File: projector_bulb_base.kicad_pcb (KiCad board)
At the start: 2 copper layers, 31 x 31 mm, 11 parts, among them J1 AC_1, J10 mount_2, J3 AC_2, J9 mount_1

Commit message: Revision 2, still needs documentation and things
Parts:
- C1, C2: footprint Capacitor_THT:CP_Radial_D16.0mm_P7.50mm -> Capacitor_THT:CP_Radial_D12.5mm_P5.00mm
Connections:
- J10 pad 1: Net-(J10-Pad1) -> (no net)
- J9 pad 1: Net-(J9-Pad1) -> (no net)
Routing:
- net GND: track 15.8 -> 30.3 mm

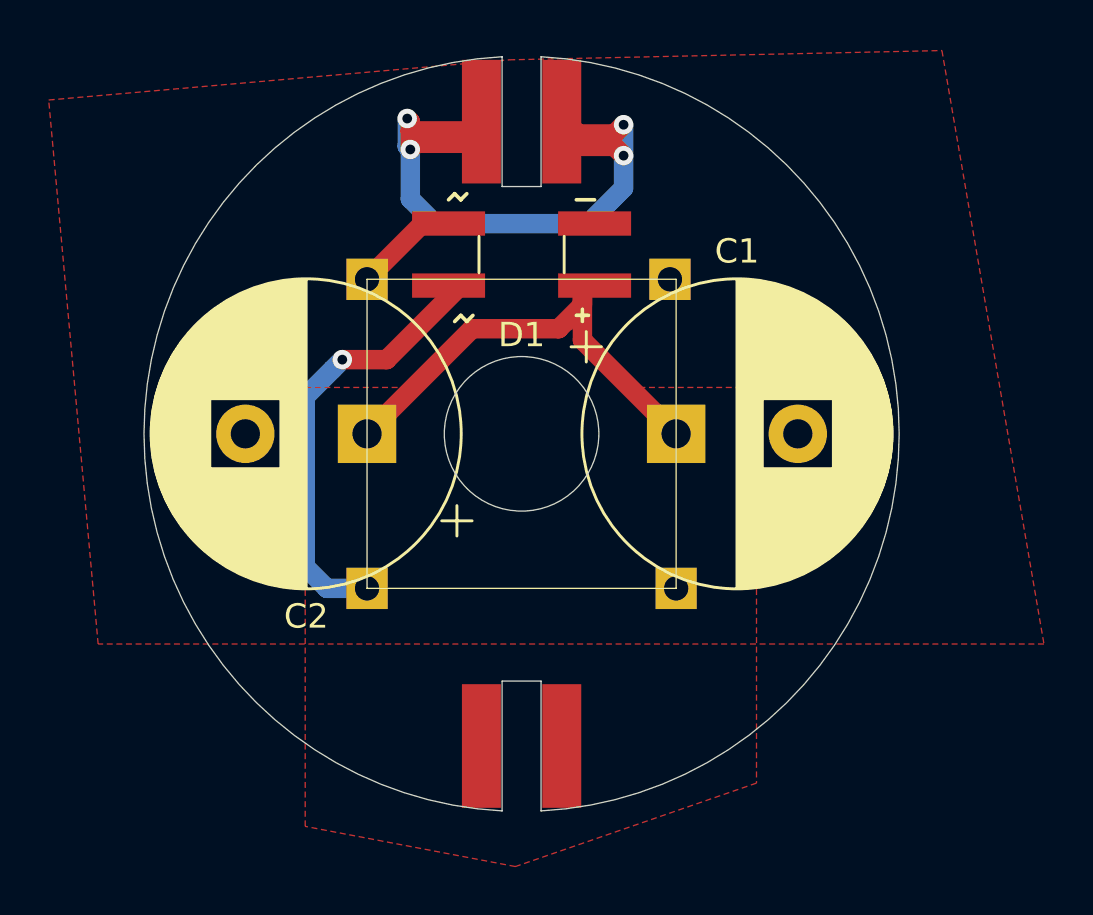
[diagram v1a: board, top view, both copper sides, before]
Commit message: Much progress on Aluminum PCB
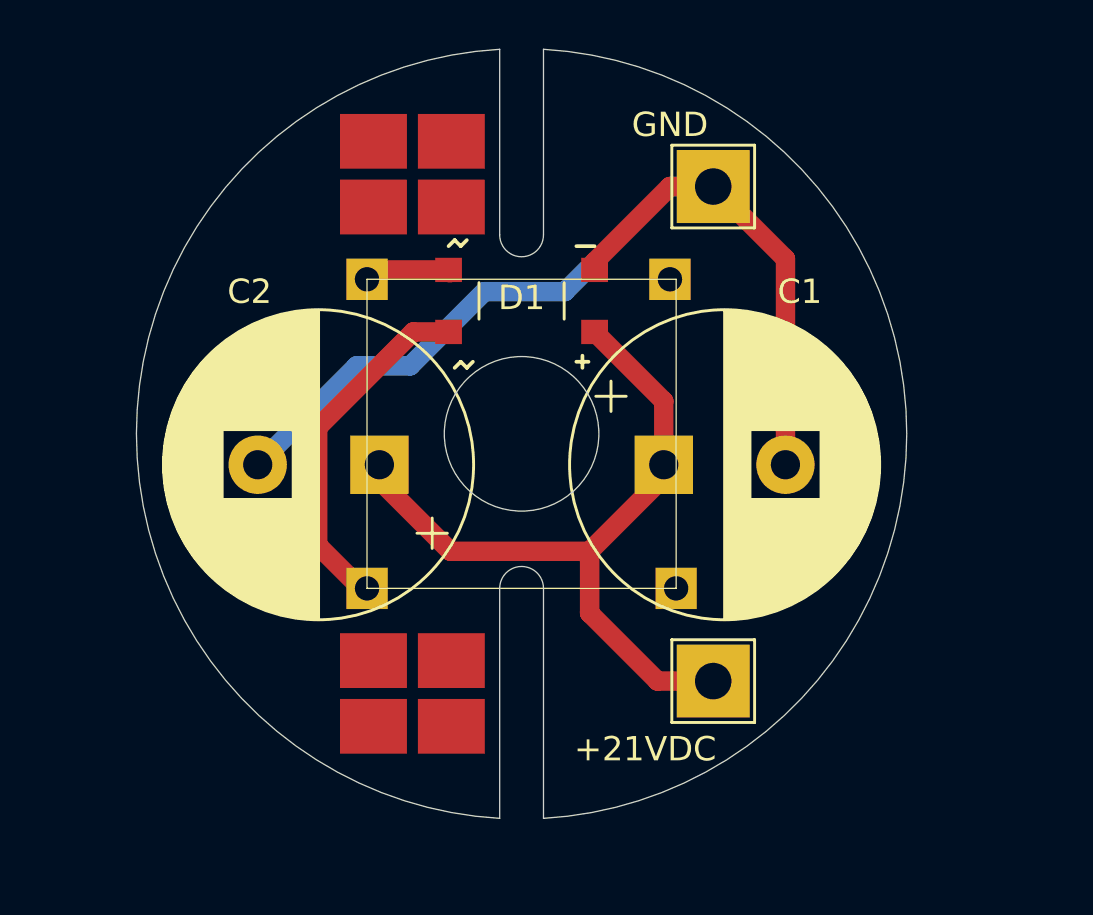
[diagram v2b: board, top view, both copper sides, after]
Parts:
- removed REF** (x4): angle_joint, projector_bulb:angle_joint
- added +21VDC: to_upright_+, TestPoint:TestPoint_THTPad_3.0x3.0mm_Drill1.5mm, F.Cu at (84.1, 86.4)
- added GND: to_upright_-, TestPoint:TestPoint_THTPad_3.0x3.0mm_Drill1.5mm, F.Cu at (84.1, 66.0)
- added J11: mount_2, projector_bulb:wuerth_7466303R, F.Cu at (71.7, 65.5)
- added J12: mount_1, projector_bulb:wuerth_7466303R, F.Cu at (71.7, 86.9)
- C1, C2: value 2200u -> 1000μ
- moved D1 1.91 mm to (76.2, 70.7)
- moved C2 1.37 mm to (70.4, 77.5)
- moved C1 1.37 mm to (82.0, 77.5)
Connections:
- net GND renamed GND_BASE
- net Net-(C1-Pad1) renamed VIN_BASE
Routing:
- net GND_BASE: track 30.3 -> 42.6 mm, vias 4 -> 0
- net VIN_BASE: track 19.5 -> 29.3 mm
- net Net-(D1-Pad4): track 18.2 -> 14.6 mm, vias 1 -> 0
- net Net-(D1-Pad3): track 4.80 -> 3.61 mm
- removed copper zone on F.Cu, net GND_BASE
- removed copper zone on F.Cu, net VIN_BASE
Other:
- board size 31 x 31 mm -> 31.7 x 31.6 mm

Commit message: Add test points, replaced some expensive components with cheaper alternatives
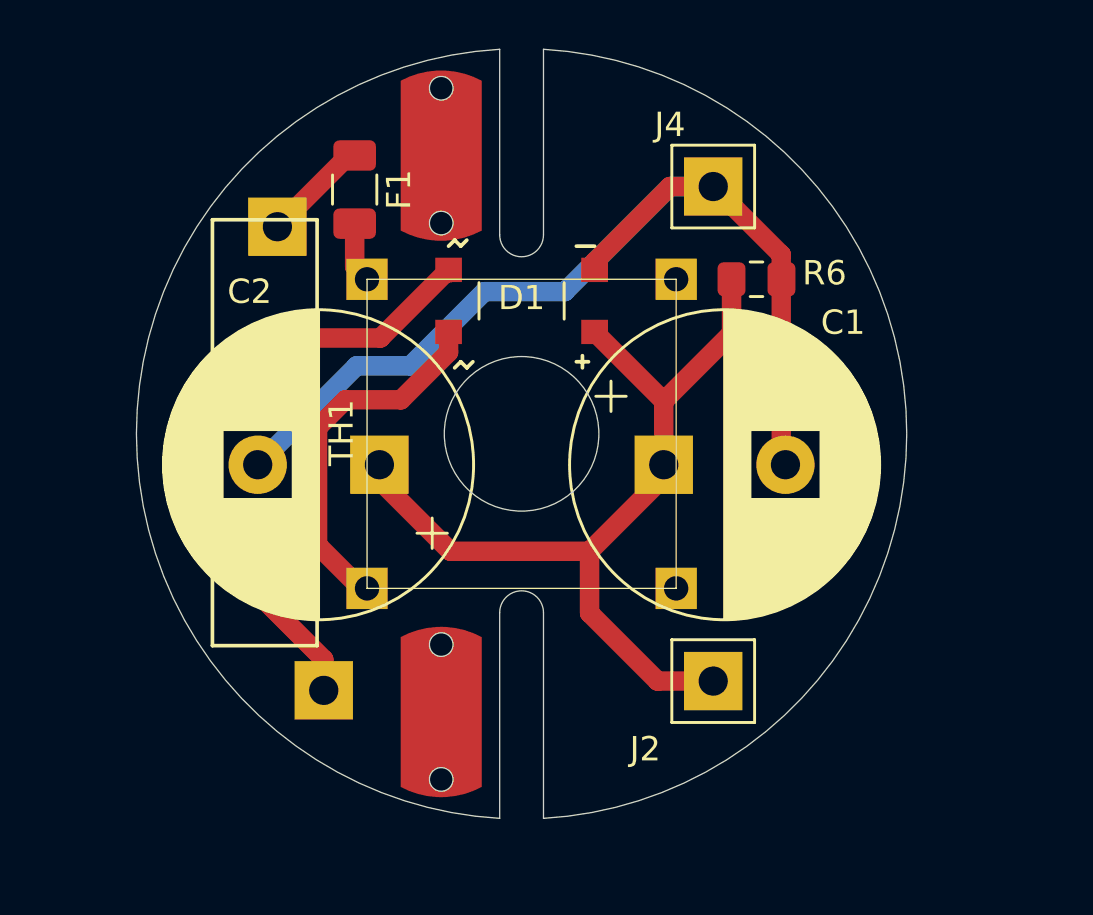
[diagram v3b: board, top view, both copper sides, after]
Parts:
- removed J1: AC_1, Connector_PinSocket_2.54mm:PinSocket_1x01_P2.54mm_Vertical
- removed J10: mount_2, Connector_PinSocket_2.54mm:PinSocket_1x01_P2.54mm_Vertical
- removed J11: mount_2, projector_bulb:wuerth_7466303R
- removed J12: mount_1, projector_bulb:wuerth_7466303R
- removed J3: AC_2, Connector_PinSocket_2.54mm:PinSocket_1x01_P2.54mm_Vertical
- removed J9: mount_1, Connector_PinSocket_2.54mm:PinSocket_1x01_P2.54mm_Vertical
- added F1: Fuse, Fuse:Fuse_1206_3216Metric, F.Cu at (69.3, 66.2)
- added H1: MountingHole, projector_bulb:wuerth_7466310R, F.Cu at (72.9, 64.8)
- added H2: MountingHole, projector_bulb:wuerth_7466310R, F.Cu at (72.9, 87.6)
- added LA1: Lamp, projector_bulb:GX17q, B.Cu at (76.2, 76.2)
- added R6: 1M, Resistor_SMD:R_0805_2012Metric_Pad1.15x1.40mm_HandSolder, F.Cu at (85.9, 69.8)
- added TH1: Thermistor_NTC, Varistor:RV_Disc_D21.5mm_W4.3mm_P10mm, F.Cu at (64.9, 81.2)
- renumbered +21VDC to J2, GND to J4
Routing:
- net Net-(D1-Pad3): track 3.61 -> 26.6 mm
- net VIN_BASE: track 29.3 -> 35.5 mm
- net Net-(F1-Pad1): track 0.00 -> 4.39 mm
- net Net-(F1-Pad2): track 0.00 -> 2.50 mm
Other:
- outline, holes or cut-outs redrawn

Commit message: BOM and readme updated
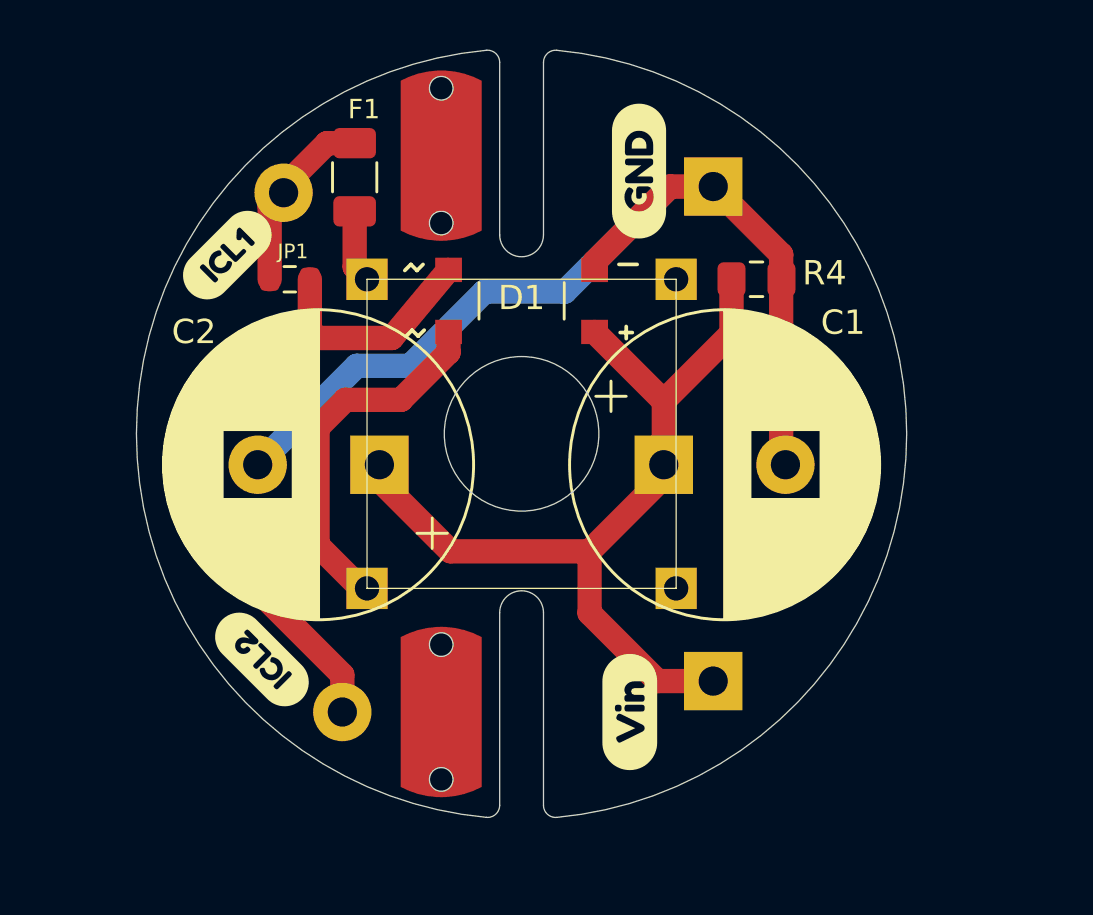
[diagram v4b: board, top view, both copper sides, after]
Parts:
- added JP1: ICL Bypass, Resistor_SMD:R_0603_1608Metric, F.Cu at (66.7, 69.8)
- added svg2mod: G***, label, F.Cu at (81.0, 65.4)
- added svg2mod: G***, label, F.Cu at (80.6, 87.6)
- added svg2mod: G***, label, F.Cu at (65.5, 85.5)
- added svg2mod: G***, label, F.Cu at (63.8, 70.0)
- D1: value D_Bridge_+-AA -> Bridge Rectifier
- moved TH1 0.89 mm to (64.9, 82.0)
- moved F1 0.50 mm to (69.3, 65.7)
- renumbered J2 to J1, J4 to J2, R6 to R4
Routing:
- net Net-(D1-Pad3): track 26.6 -> 30.3 mm
- net Net-(F1-Pad1): track 4.39 -> 7.27 mm
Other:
- board size 31.7 x 31.6 mm -> 31.6 x 31.5 mm
- net class Base Track added: clearance 0.25, trace_width 1, via_dia 0.8, via_drill 0.4
- rule pad_to_mask_clearance: 0.05 -> 0

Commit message: Locking in revision 3 finally; moved the optional ICL to a place where I can treat it like a test point
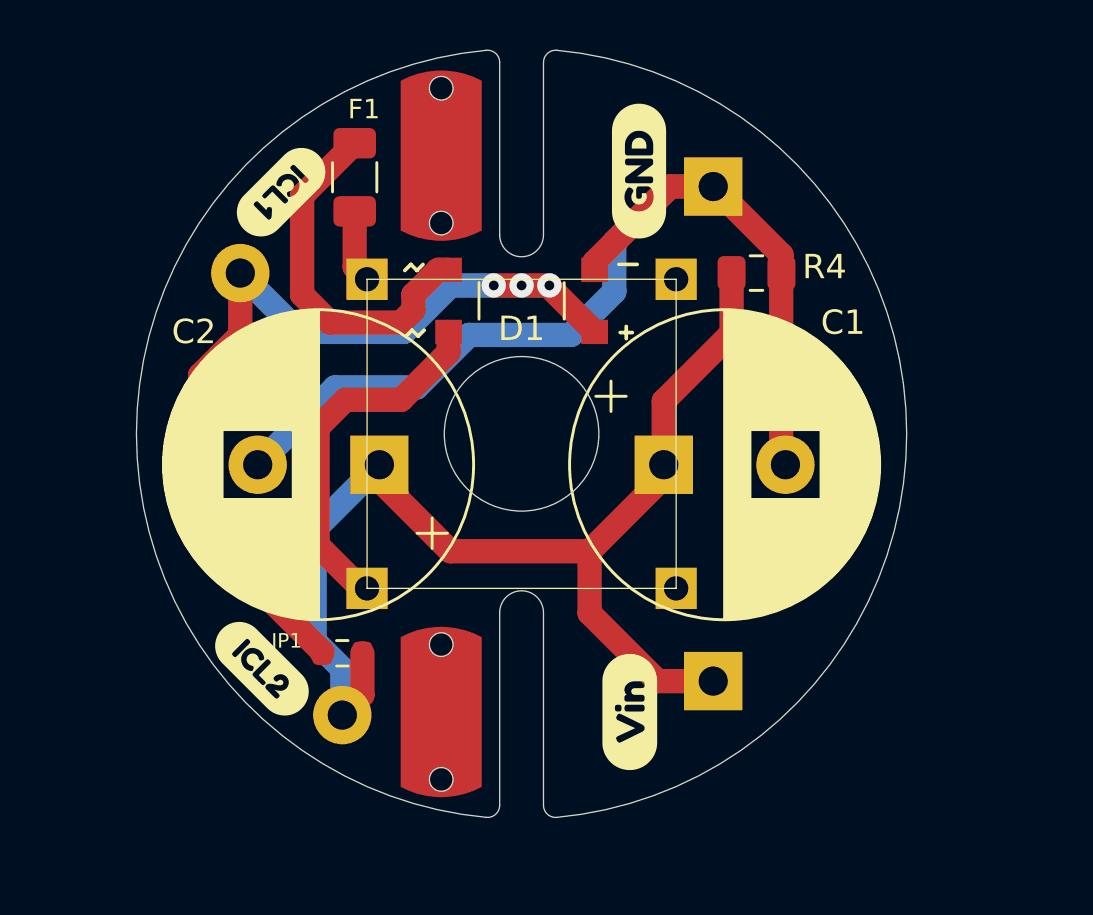
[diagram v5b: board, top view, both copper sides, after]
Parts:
- moved JP1 15.5 mm to (68.8, 85.2)
- moved svg2mod 5.64 mm to (66.7, 65.2), turned to 180 degrees
- moved svg2mod 0.38 mm to (65.5, 85.9), turned to 270 degrees
- moved R4 0.25 mm to (85.9, 69.6)
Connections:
- D1 pad 1: VIN_BASE -> Net-(D1-Pad1)
- F1 pad 1: Net-(F1-Pad1) -> Net-(D1-Pad3)
- JP1 pad 1: Net-(F1-Pad1) -> Net-(D1-Pad1)
- JP1 pad 2: Net-(D1-Pad3) -> VIN_BASE
- TH1 pad 1: Net-(D1-Pad3) -> VIN_BASE
- TH1 pad 2: Net-(F1-Pad1) -> Net-(D1-Pad1)
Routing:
- net Net-(D1-Pad1): track 0.00 -> 37.8 mm, vias 0 -> 3
- net Net-(D1-Pad3): track 30.3 -> 14.9 mm
- net VIN_BASE: track 35.5 -> 46.5 mm
- net Net-(F1-Pad1): track 7.27 -> 0.00 mm
- net GND_BASE: track 42.6 -> 43.8 mm

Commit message: Changed all references of 7466310R to 7466313R
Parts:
- H1, H2: footprint projector_bulb:wuerth_7466310R -> projector_bulb:wuerth_7466313R
